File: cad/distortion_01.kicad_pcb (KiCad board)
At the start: 2 copper layers, 54 x 99.8 mm, 103 parts, among them CON101 Ext_PSU, J101 JACK_IN, J102 JACK_OUT, P101 Battery_conn, P102 BYPASS_SWITCH, P103 CONN_01X03, P104 CONN_01X03, P105 CONN_01X03, P106 CONN_01X03, Q101 BS170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

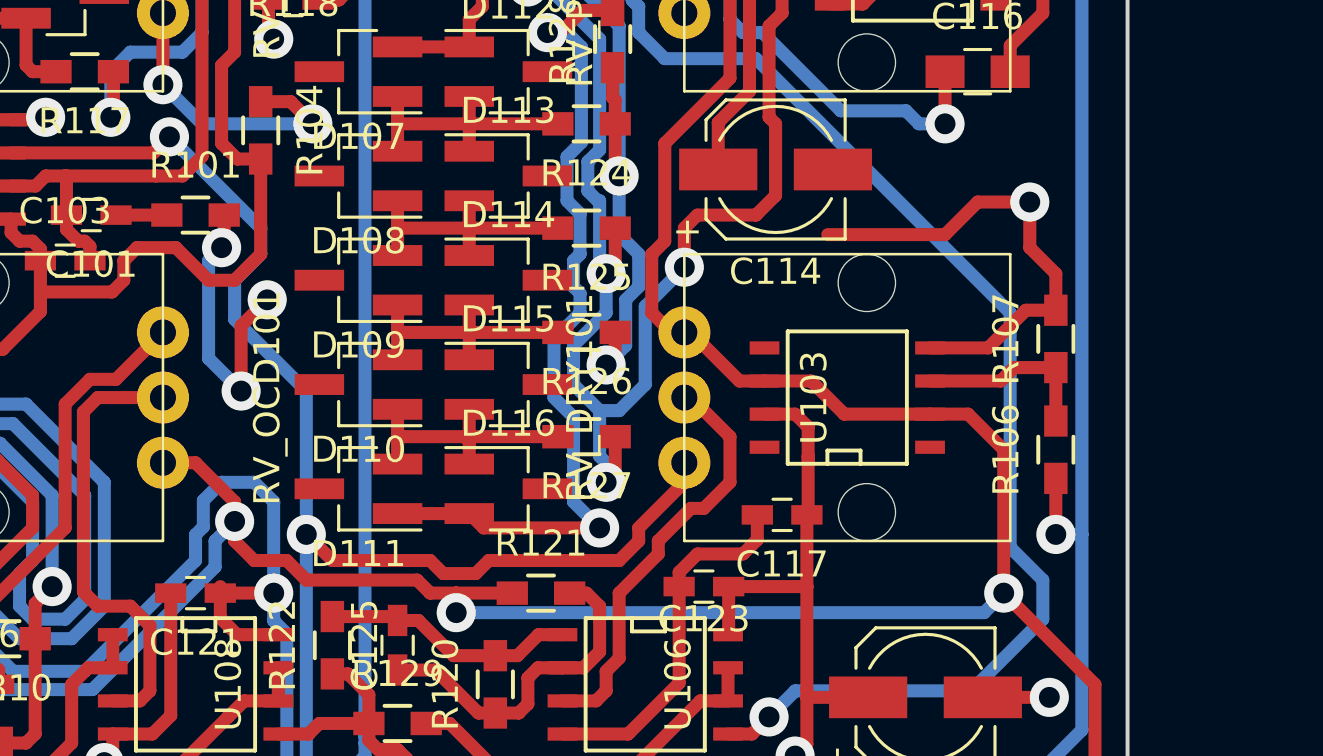
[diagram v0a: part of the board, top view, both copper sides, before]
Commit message: Added LTspice simulation.
Added 10n cap on OCD output.
Added 10u cap on Vref for HF stability.
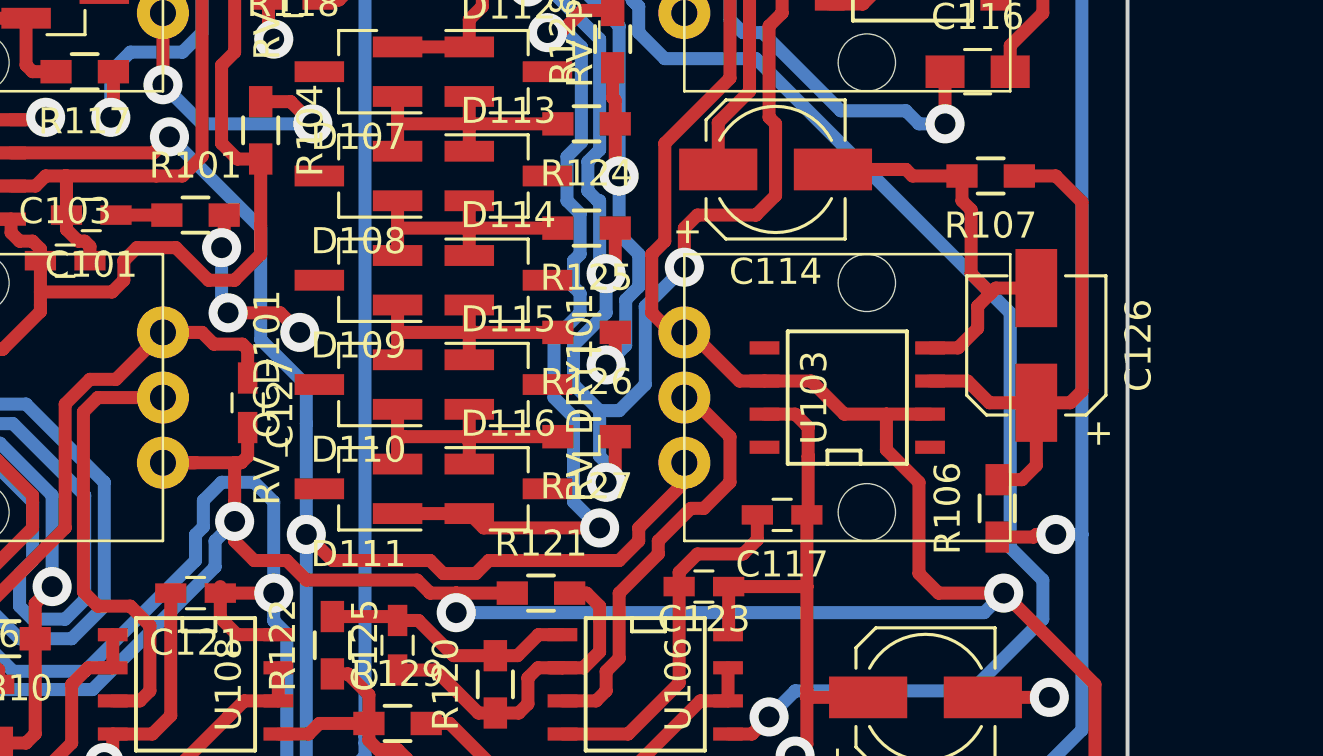
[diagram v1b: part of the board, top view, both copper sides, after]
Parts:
- added C126: 10u, Capacitors_SMD:CP_Elec_5x4.5, F.Cu at (102.0, 88.8)
- added C127: 10n, Capacitors_SMD:C_0603_HandSoldering, F.Cu at (71.8, 91.0)
- moved R107 6.73 mm to (100.2, 82.2), turned to 180 degrees
- moved R106 3.18 mm to (100.5, 95.0)
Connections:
- Q101 pad 2: Net-(C105-Pad2) -> (no net)
- Q102 pad 2: VCOM -> (no net)
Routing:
- net Net-(C126-Pad1): track 7.09 -> 20.5 mm
- net GND: track 152.9 -> 145.2 mm, vias 20 -> 19
- net VCOM: track 224.2 -> 230.0 mm
- net Net-(C109-Pad2): track 25.9 -> 30.6 mm
- net /audio_fx_in: track 59.1 -> 58.3 mm

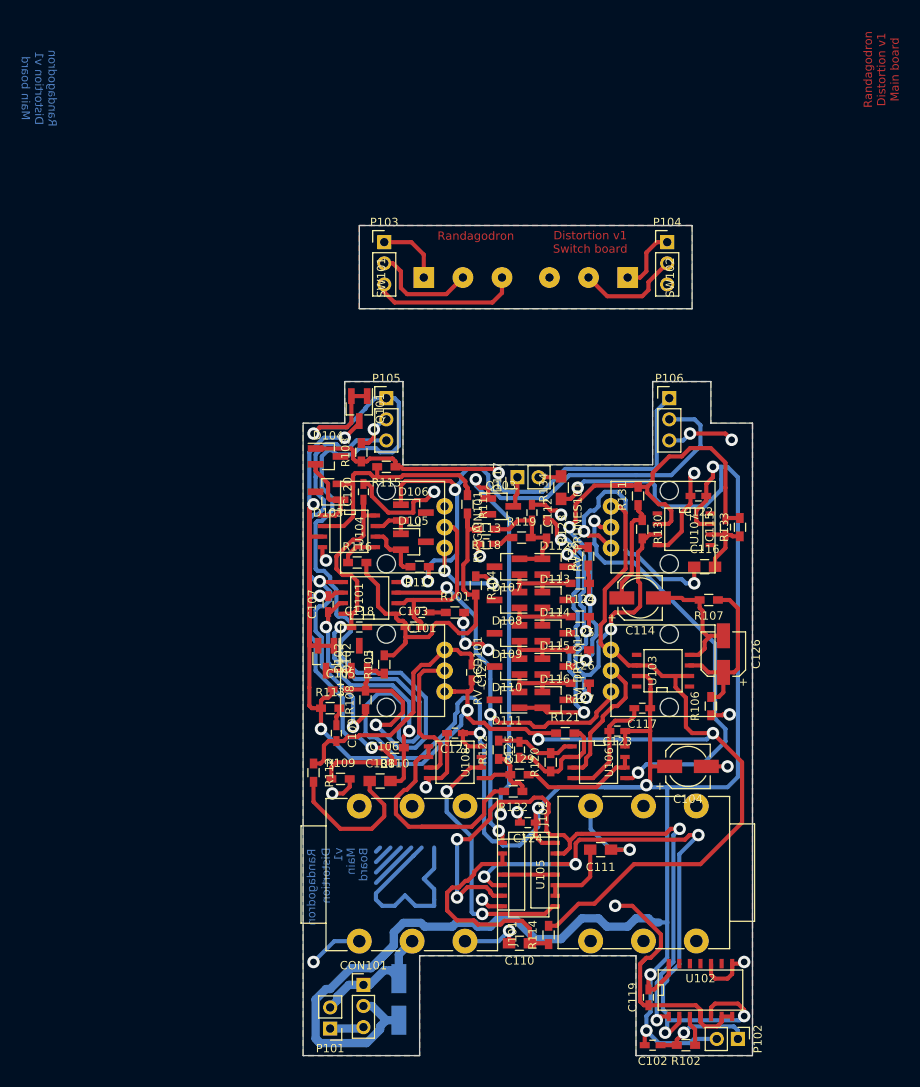
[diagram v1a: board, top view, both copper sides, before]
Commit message: Updated PCB number to v2.
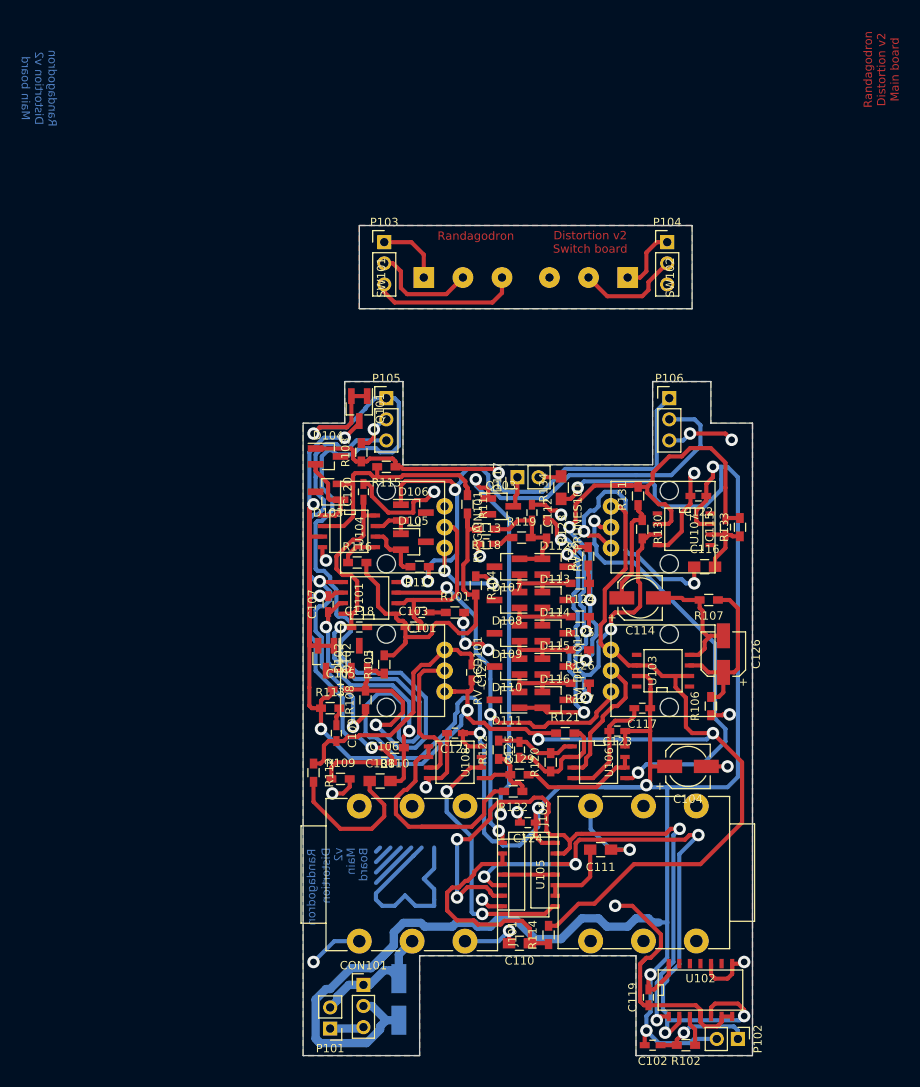
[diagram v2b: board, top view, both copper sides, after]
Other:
- board text added: "Distortion v2 Switch board"
- board text added: "Randagodron Distortion v2 Main board"
- board text added: "v2"
- board text removed: "Distortion v1 Switch board"
- board text removed: "Randagodron Distortion v1 Main board"
- board text removed: "v1"
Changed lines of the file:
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@@
   (general
     (links 205)
-    (no_connects 27)
-    (area 51.424999 37.174999 105.575001 137.075001)
+    (no_connects 3)
+    (area 17.15 12.55 263.75 141.080952)
     (thickness 1.6)
     (drawings 86)
@@
     (effects (font (size 1 1) (thickness 0.2)) (justify left mirror))
   )
-  (gr_text v1 (at 55.75 112 90) (layer B.Cu)
+  (gr_text v2 (at 55.75 112 90) (layer B.Cu)
     (effects (font (size 1 1) (thickness 0.2)) (justify left mirror))
   )
@@
   )
   (gr_line (start 67.5 33.5) (end 67.5 50.25) (angle 90) (layer Eco2.User) (width 0.2))
-  (gr_text "Distortion v1\nSwitch board" (at 86 39.25) (layer F.Cu)
+  (gr_text "Distortion v2\nSwitch board" (at 86 39.25) (layer F.Cu)
     (effects (font (size 1 1) (thickness 0.2)))
   )
@@
     (arrow2b (pts (xy 40.5 20.75) (xy 41.626504 20.163579)))
   )
-  (gr_text "Randagodron\nDistortion v1\nMain board" (at 19.75 20.75 270) (layer B.Cu)
+  (gr_text "Randagodron\nDistortion v2\nMain board" (at 19.75 20.75 270) (layer B.Cu)
     (effects (font (size 1 1) (thickness 0.2)) (justify mirror))
   )
@@
     (effects (font (size 1 1) (thickness 0.2)))
   )
-  (gr_text "Randagodron\nDistortion v1\nMain board" (at 121 18.5 90) (layer F.Cu)
+  (gr_text "Randagodron\nDistortion v2\nMain board" (at 121 18.5 90) (layer F.Cu)
     (effects (font (size 1 1) (thickness 0.2)))
   )

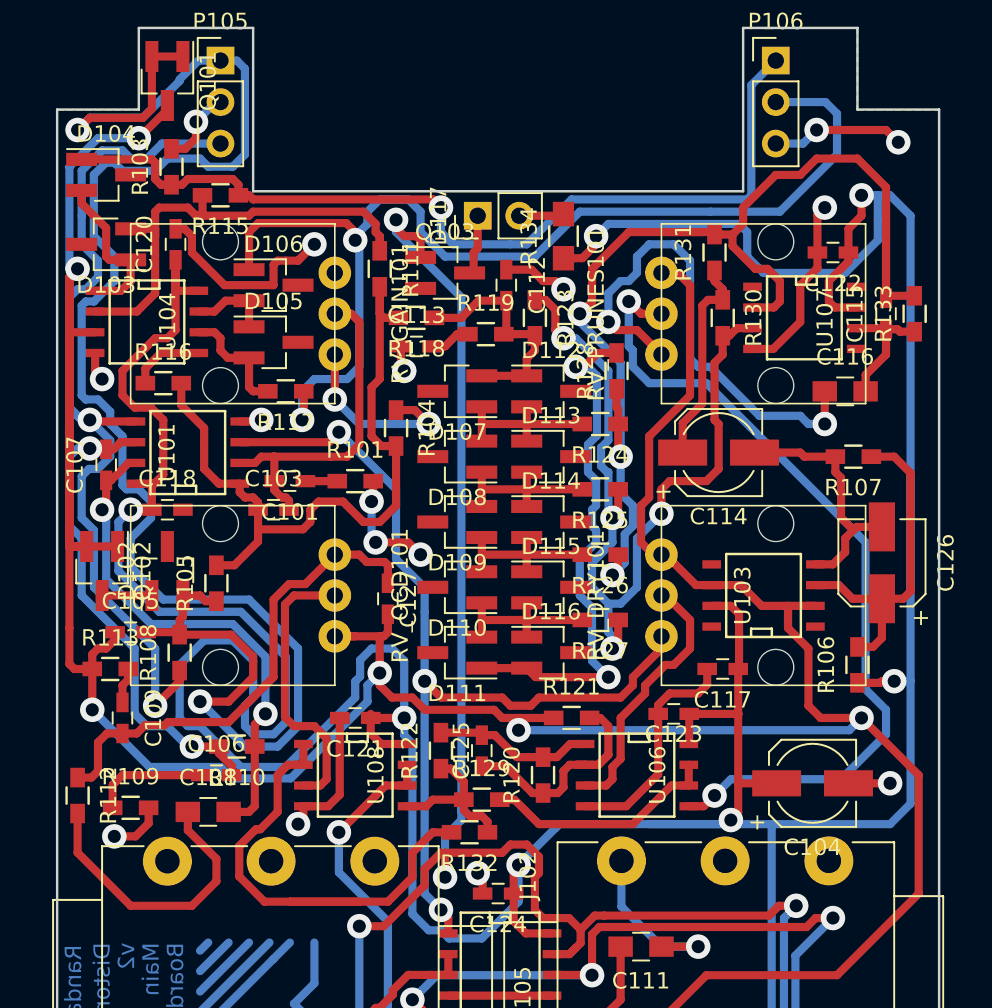
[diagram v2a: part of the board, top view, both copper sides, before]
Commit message: Corrected pots polarity (schematic and layout).
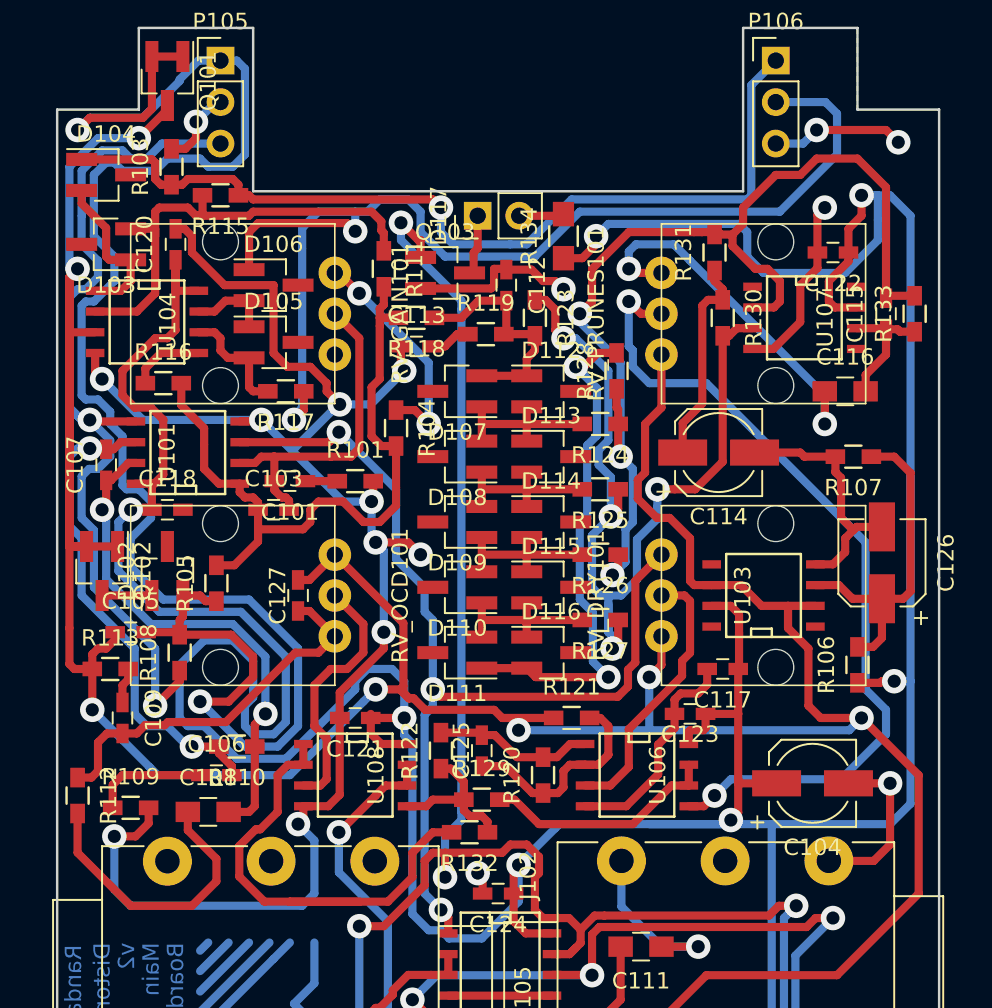
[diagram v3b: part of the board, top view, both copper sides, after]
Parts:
- moved C127 5.50 mm to (66.2, 90.8), turned to 90 degrees
- moved C123 1.00 mm to (90.2, 98.0)
- moved R111 0.25 mm to (71.5, 70.8)
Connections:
- RV_DRY101 pad 1: VCOM -> /audio_fx_in
- RV_DRY101 pad 3: /audio_fx_in -> VCOM
- RV_GAIN101 pad 1: Net-(R104-Pad1) -> (no net)
- RV_GAIN101 pad 3: (no net) -> Net-(R104-Pad1)
- RV_OCD101 pad 1: VCOM -> Net-(C109-Pad2)
- RV_OCD101 pad 3: Net-(C109-Pad2) -> VCOM
- RV_PRUNES101 pad 1: VCOM -> Net-(C116-Pad1)
- RV_PRUNES101 pad 3: Net-(C116-Pad1) -> VCOM
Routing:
- net GND: track 145.2 -> 225.7 mm, vias 19 -> 20
- net Net-(C116-Pad1): track 31.0 -> 22.9 mm
- net Net-(C109-Pad2): track 30.6 -> 23.3 mm
- net /audio_fx_in: track 58.3 -> 63.1 mm
- net +9V: track 300.5 -> 296.9 mm
- net VCOM: track 230.0 -> 232.9 mm, vias 6 -> 7
- net Net-(R104-Pad1): track 11.5 -> 14.1 mm
- net /audio_ocd_out: track 17.4 -> 15.7 mm
- net Net-(R123-Pad1): track 52.7 -> 54.2 mm
- net Net-(C101-Pad2): track 21.8 -> 20.4 mm
- net Net-(D106-Pad1): track 68.0 -> 69.2 mm
- net /bypass_cmd: track 124.8 -> 123.6 mm
- net Net-(D111-Pad1): track 32.7 -> 31.6 mm
- net /audio_gain: track 44.0 -> 43.3 mm
- net Net-(RV_DRY101-Pad2): track 16.2 -> 16.8 mm
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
